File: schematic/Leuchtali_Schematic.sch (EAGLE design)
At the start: 71 parts, among them IC2 LT1618EMS#PBF, IC3 LT1618EMS#PBF, IC4 LT1618EMS#PBF, IC5 LT1618EMS#PBF

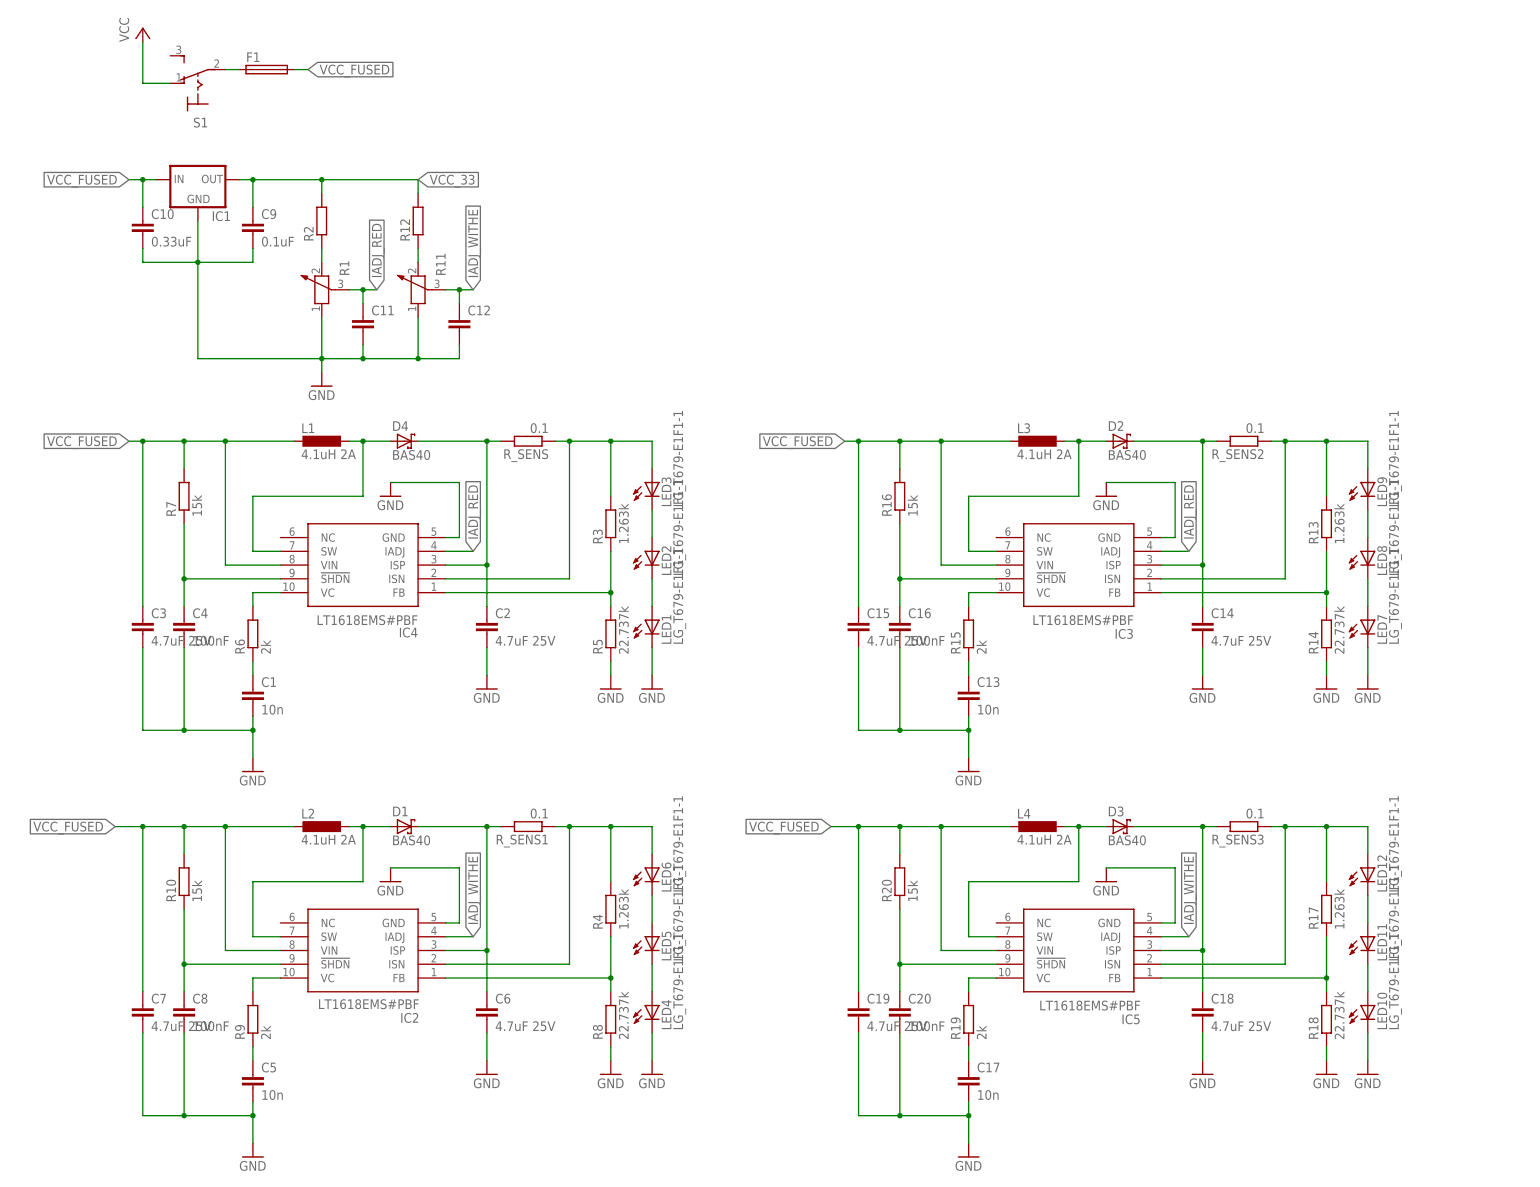
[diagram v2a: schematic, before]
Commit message: Added diode datasheet and updated schematic.
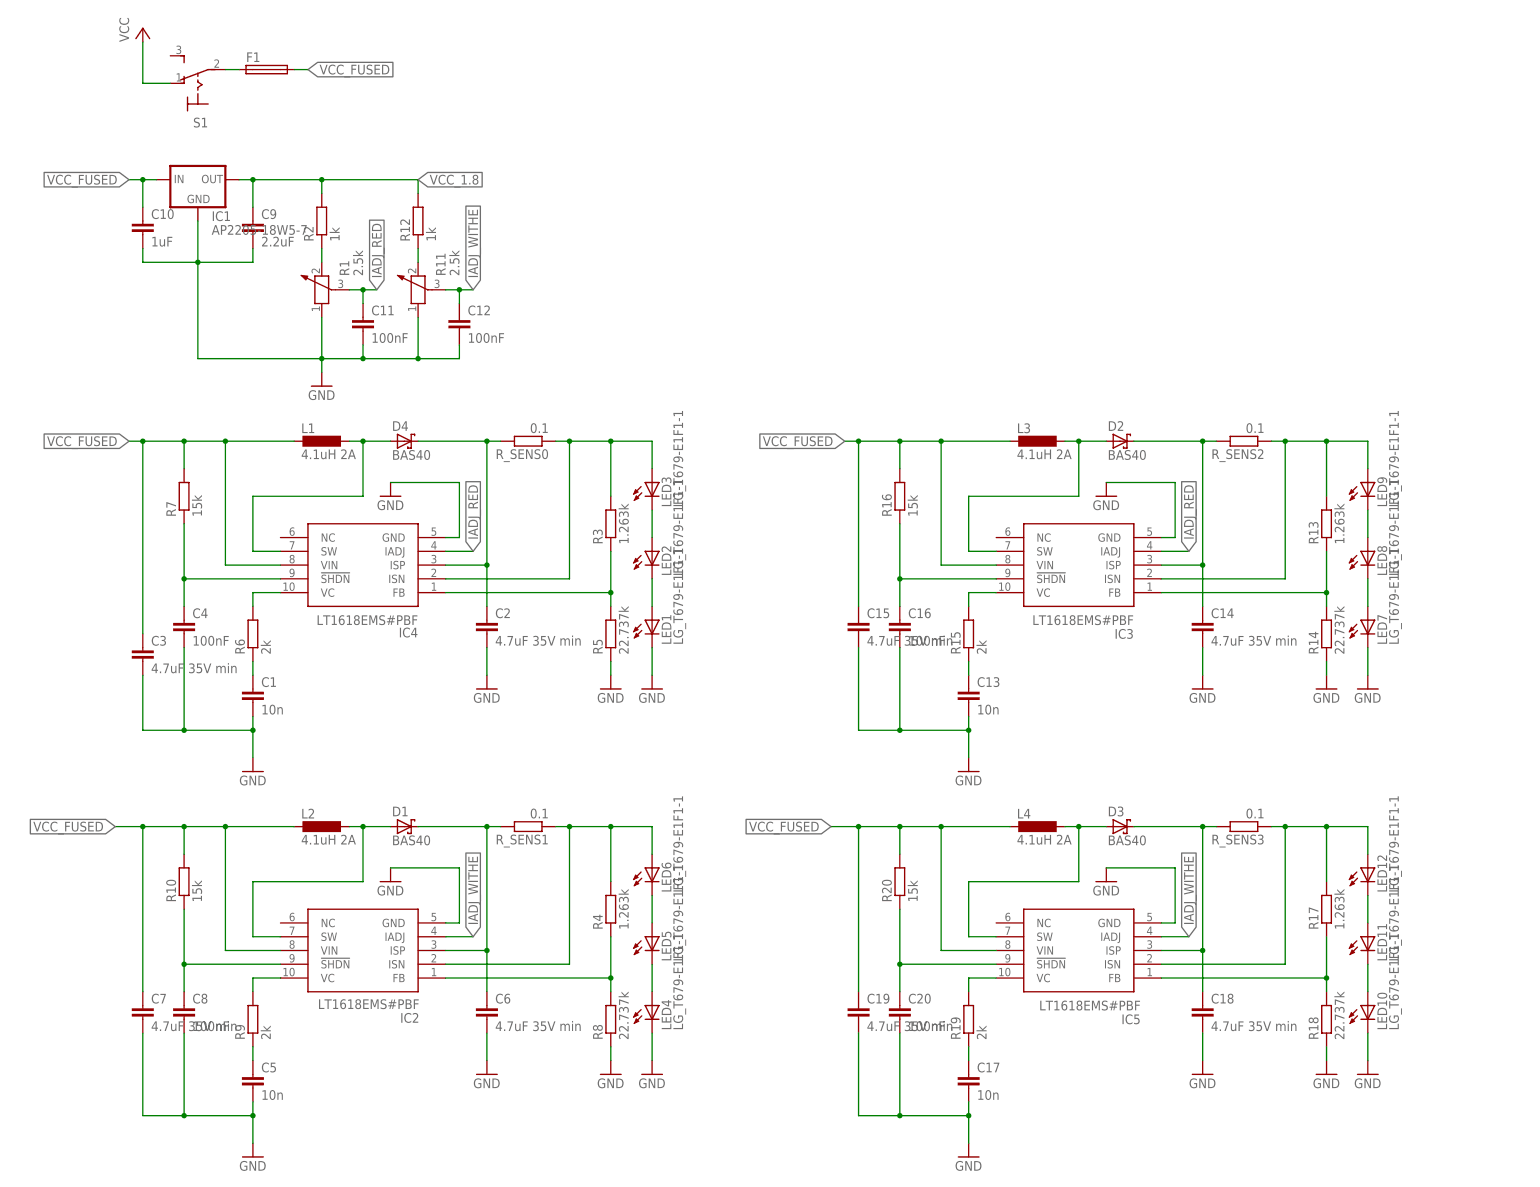
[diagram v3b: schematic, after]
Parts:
- C10: value 0.33uF -> 1uF
- C11, C12: value (none) -> 100nF
- C14, C15, C18, C19, C2, C3, C6, C7: value 4.7uF 25V -> 4.7uF 35V min
- C9: value 0.1uF -> 2.2uF
- IC1: value (none) -> AP2205-18W5-7
- R1, R11: value (none) -> 2.5k
- R12, R2: value (none) -> 1k
- renumbered R_SENS to R_SENS0
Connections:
- net VCC_33 renamed VCC_1.8
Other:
- moved on the sheet: C3
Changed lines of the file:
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@@
 <part name="R3" library="rcl" deviceset="R-EU_" device="R0805" value="1.263k"/>
 <part name="R5" library="rcl" deviceset="R-EU_" device="R0805" value="22.737k"/>
-<part name="R_SENS" library="rcl" deviceset="R-EU_" device="R0805" value="0.1"/>
+<part name="R_SENS0" library="rcl" deviceset="R-EU_" device="R0805" value="0.1"/>
 <part name="D4" library="diode" deviceset="BAS40" device=""/>
 <part name="P+1" library="supply1" deviceset="VCC" device=""/>
@@
 <part name="R6" library="rcl" deviceset="R-EU_" device="R0805" value="2k"/>
 <part name="C1" library="rcl" deviceset="C-EU" device="C0805" value="10n"/>
-<part name="C2" library="rcl" deviceset="C-EU" device="C0805" value="4.7uF 25V"/>
+<part name="C2" library="rcl" deviceset="C-EU" device="C0805" value="4.7uF 35V min"/>
 <part name="GND8" library="supply1" deviceset="GND" device=""/>
-<part name="C3" library="rcl" deviceset="C-EU" device="C0805" value="4.7uF 25V"/>
+<part name="C3" library="rcl" deviceset="C-EU" device="C0805" value="4.7uF 35V min"/>
 <part name="C4" library="rcl" deviceset="C-EU" device="C0805" value="100nF"/>
 <part name="R7" library="rcl" deviceset="R-EU_" device="R0805" value="15k"/>
 <part name="S1" library="switch" deviceset="320-916" device=""/>
 <part name="F1" library="fuse" deviceset="GSH15" device=""/>
-<part name="R1" library="rcl" deviceset="POTENTIOMETER_" device="PT-10"/>
-<part name="IC1" library="v-reg" deviceset="78LXX" device=""/>
+<part name="R1" library="rcl" deviceset="POTENTIOMETER_" device="PT-10" value="2.5k"/>
+<part name="IC1" library="v-reg" deviceset="78LXX" device="" value="AP2205-18W5-7"/>
 <part name="GND1" library="supply1" deviceset="GND" device=""/>
-<part name="R2" library="rcl" deviceset="R-EU_" device="R0805"/>
+<part name="R2" library="rcl" deviceset="R-EU_" device="R0805" value="1k"/>
 <part name="IC2" library="LT1618EMS" deviceset="LT1618EMS#PBF" device=""/>
 <part name="GND2" library="supply1" deviceset="GND" device=""/>
@@
 <part name="R9" library="rcl" deviceset="R-EU_" device="R0805" value="2k"/>
 <part name="C5" library="rcl" deviceset="C-EU" device="C0805" value="10n"/>
-<part name="C6" library="rcl" deviceset="C-EU" device="C0805" value="4.7uF 25V"/>
+<part name="C6" library="rcl" deviceset="C-EU" device="C0805" value="4.7uF 35V min"/>
 <part name="GND11" library="supply1" deviceset="GND" device=""/>
-<part name="C7" library="rcl" deviceset="C-EU" device="C0805" value="4.7uF 25V"/>
+<part name="C7" library="rcl" deviceset="C-EU" device="C0805" value="4.7uF 35V min"/>
 <part name="C8" library="rcl" deviceset="C-EU" device="C0805" value="100nF"/>
 <part name="R10" library="rcl" deviceset="R-EU_" device="R0805" value="15k"/>
-<part name="R11" library="rcl" deviceset="POTENTIOMETER_" device="PT-10"/>
-<part name="R12" library="rcl" deviceset="R-EU_" device="R0805"/>
-<part name="C9" library="rcl" deviceset="C-EU" device="025-024X044" value="0.1uF"/>
-<part name="C10" library="rcl" deviceset="C-EU" device="025-024X044" value="0.33uF"/>
-<part name="C11" library="rcl" deviceset="C-EU" device="025-024X044"/>
-<part name="C12" library="rcl" deviceset="C-EU" device="025-024X044"/>
+<part name="R11" library="rcl" deviceset="POTENTIOMETER_" device="PT-10" value="2.5k"/>
+<part name="R12" library="rcl" deviceset="R-EU_" device="R0805" value="1k"/>
+<part name="C9" library="rcl" deviceset="C-EU" device="025-024X044" value="2.2uF"/>
+<part name="C10" library="rcl" deviceset="C-EU" device="025-024X044" value="1uF"/>
+<part name="C11" library="rcl" deviceset="C-EU" device="025-024X044" value="100nF"/>
+<part name="C12" library="rcl" deviceset="C-EU" device="025-024X044" value="100nF"/>
 <part name="IC3" library="LT1618EMS" deviceset="LT1618EMS#PBF" device=""/>
 <part name="GND12" library="supply1" deviceset="GND" device=""/>
@@
 <part name="R15" library="rcl" deviceset="R-EU_" device="R0805" value="2k"/>
 <part name="C13" library="rcl" deviceset="C-EU" device="C0805" value="10n"/>
-<part name="C14" library="rcl" deviceset="C-EU" device="C0805" value="4.7uF 25V"/>
+<part name="C14" library="rcl" deviceset="C-EU" device="C0805" value="4.7uF 35V min"/>
 <part name="GND16" library="supply1" deviceset="GND" device=""/>
-<part name="C15" library="rcl" deviceset="C-EU" device="C0805" value="4.7uF 25V"/>
+<part name="C15" library="rcl" deviceset="C-EU" device="C0805" value="4.7uF 35V min"/>
 <part name="C16" library="rcl" deviceset="C-EU" device="C0805" value="100nF"/>
 <part name="R16" library="rcl" deviceset="R-EU_" device="R0805" value="15k"/>
@@
 <part name="R19" library="rcl" deviceset="R-EU_" device="R0805" value="2k"/>
 <part name="C17" library="rcl" deviceset="C-EU" device="C0805" value="10n"/>
-<part name="C18" library="rcl" deviceset="C-EU" device="C0805" value="4.7uF 25V"/>
+<part name="C18" library="rcl" deviceset="C-EU" device="C0805" value="4.7uF 35V min"/>
 <part name="GND21" library="supply1" deviceset="GND" device=""/>
-<part name="C19" library="rcl" deviceset="C-EU" device="C0805" value="4.7uF 25V"/>
+<part name="C19" library="rcl" deviceset="C-EU" device="C0805" value="4.7uF 35V min"/>
 <part name="C20" library="rcl" deviceset="C-EU" device="C0805" value="100nF"/>
 <part name="R20" library="rcl" deviceset="R-EU_" device="R0805" value="15k"/>
@@
 <instance part="R3" gate="G$1" x="106.68" y="119.38" rot="R90"/>
 <instance part="R5" gate="G$1" x="106.68" y="99.06" rot="R90"/>
-<instance part="R_SENS" gate="G$1" x="91.44" y="134.62" rot="R180"/>
+<instance part="R_SENS0" gate="G$1" x="91.44" y="134.62" rot="R180"/>
 <instance part="D4" gate="1" x="68.58" y="134.62"/>
 <instance part="P+1" gate="VCC" x="20.32" y="210.82"/>
@@
 <instance part="C2" gate="G$1" x="83.82" y="101.6"/>
 <instance part="GND8" gate="1" x="83.82" y="88.9"/>
-<instance part="C3" gate="G$1" x="20.32" y="101.6"/>
+<instance part="C3" gate="G$1" x="20.32" y="96.52"/>
 <instance part="C4" gate="G$1" x="27.94" y="101.6"/>
 <instance part="R7" gate="G$1" x="27.94" y="124.46" rot="R90"/>
@@
 <pinref part="C3" gate="G$1" pin="2"/>
 <wire x1="40.64" y1="81.28" x2="40.64" y2="83.82" width="0.1524" layer="91"/>
-<wire x1="20.32" y1="96.52" x2="20.32" y2="81.28" width="0.1524" layer="91"/>
+<wire x1="20.32" y1="91.44" x2="20.32" y2="81.28" width="0.1524" layer="91"/>
 <wire x1="20.32" y1="81.28" x2="27.94" y2="81.28" width="0.1524" layer="91"/>
 <junction x="40.64" y="81.28"/>
@@
 <pinref part="IC4" gate="G$1" pin="ISP"/>
 <wire x1="83.82" y1="111.76" x2="76.2" y2="111.76" width="0.1524" layer="91"/>
-<pinref part="R_SENS" gate="G$1" pin="2"/>
+<pinref part="R_SENS0" gate="G$1" pin="2"/>
 <pinref part="D4" gate="1" pin="C"/>
 <wire x1="71.12" y1="134.62" x2="83.82" y2="134.62" width="0.1524" layer="91"/>
@@
 <net name="N$18" class="0">
 <segment>
-<pinref part="R_SENS" gate="G$1" pin="1"/>
+<pinref part="R_SENS0" gate="G$1" pin="1"/>
 <pinref part="R3" gate="G$1" pin="2"/>
 <wire x1="96.52" y1="134.62" x2="99.06" y2="134.62" width="0.1524" layer="91"/>
@@
 </segment>
 </net>
-<net name="VCC_33" class="0">
+<net name="VCC_1.8" class="0">
 <segment>
 <pinref part="R2" gate="G$1" pin="2"/>
@@
 <pinref part="C3" gate="G$1" pin="1"/>
 <pinref part="R7" gate="G$1" pin="2"/>
-<wire x1="20.32" y1="104.14" x2="20.32" y2="134.62" width="0.1524" layer="91"/>
+<wire x1="20.32" y1="99.06" x2="20.32" y2="134.62" width="0.1524" layer="91"/>
 <wire x1="27.94" y1="129.54" x2="27.94" y2="134.62" width="0.1524" layer="91"/>
 <junction x="27.94" y="134.62"/>

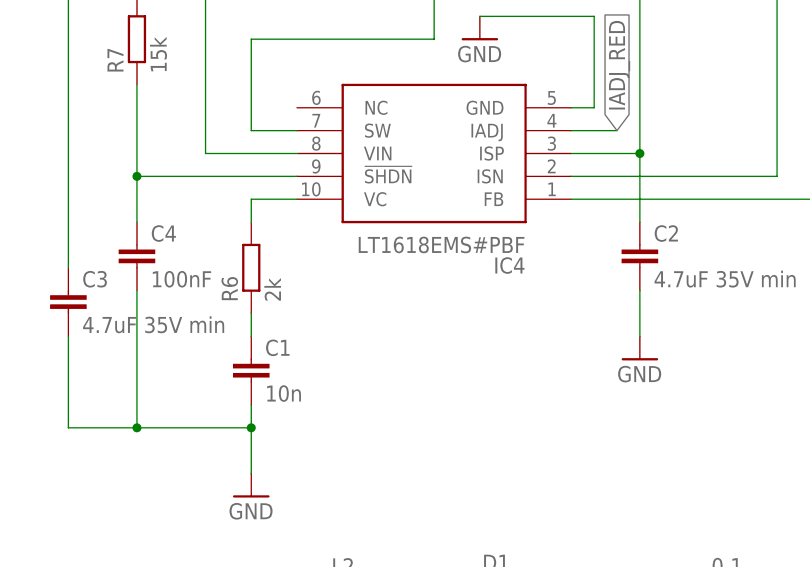
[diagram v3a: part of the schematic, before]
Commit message: added comment to the schematic
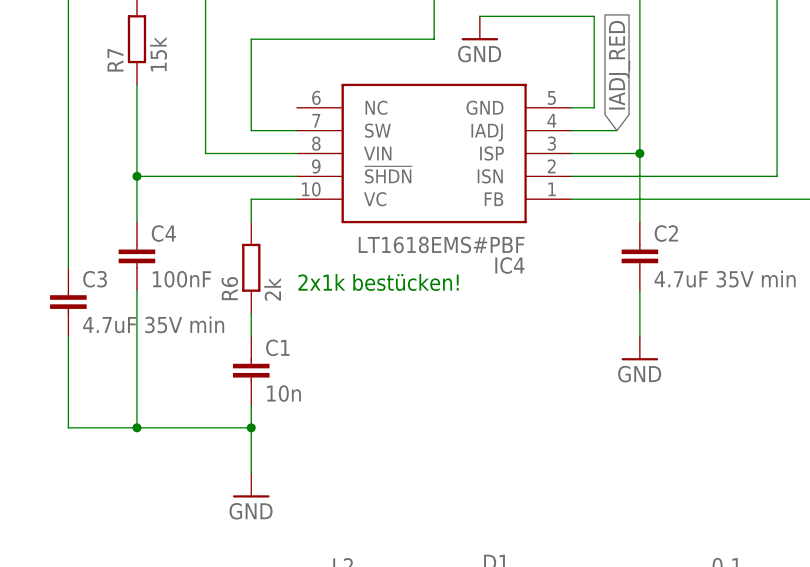
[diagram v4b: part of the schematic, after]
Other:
- note added: "2x1k bestücken!"
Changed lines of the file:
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@@
 <sheet>
 <plain>
+<text x="45.72" y="96.52" size="1.778" layer="91">2x1k bestücken!</text>
 </plain>
 <instances>
